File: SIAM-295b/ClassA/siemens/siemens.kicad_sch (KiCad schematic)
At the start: 113 parts, among them J1 PWR_IN, J2 Conn_01x08_Pin, J3 AUDIO_IN, J4 AUDIO_OUT, Q1 BC849, Q10 BCX56, Q11 BCX56, Q12 BC849, Q2 BCX56, Q3 BCX56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

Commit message: update ocb
added mounting holes, reduced width
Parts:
- removed R22: 1k2, Resistor_SMD:R_1206_3216Metric_Pad1.30x1.75mm_HandSolder, symbol Device:R
- added H1, H2, H4: MountingHole, MountingHole:MountingHole_3.2mm_M3_DIN965, symbol Mechanical:MountingHole
- added H3: MountingHole, MountingHole:MountingHole_3.2mm_M3_DIN965_Pad, symbol Mechanical:MountingHole_Pad
- added R43: 0R, Resistor_SMD:R_1206_3216Metric, symbol Device:R
- R18: value 1k3 -> 2k4
- R19: value 1k2 -> 100R
- R30: value 1k2 -> 2k4
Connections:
- net GND: now also R43.2
- net at R30.2: now also RV29.3
- new net: H3.1, R43.1

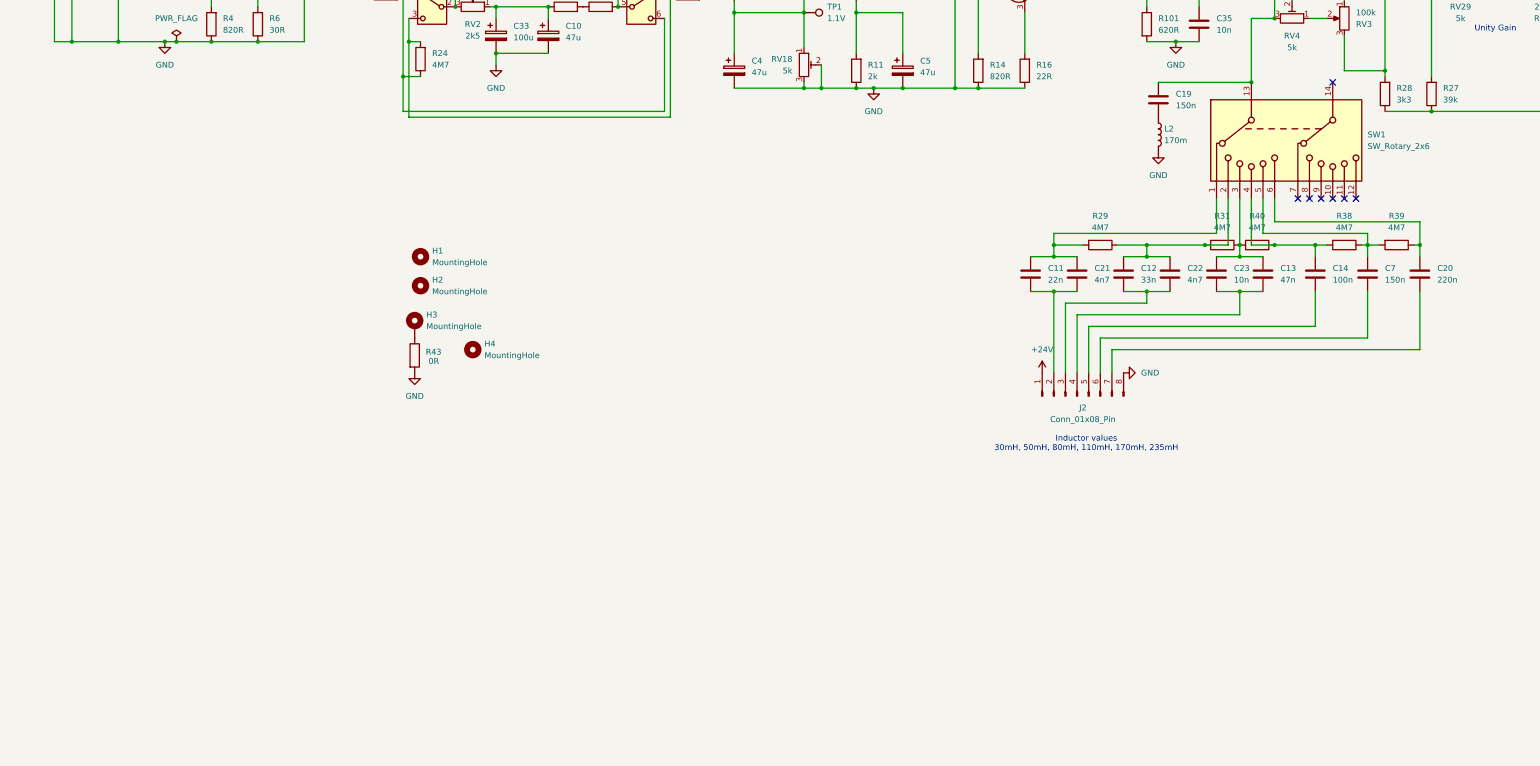
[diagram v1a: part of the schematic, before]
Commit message: added gyrator circuits
includes simulation
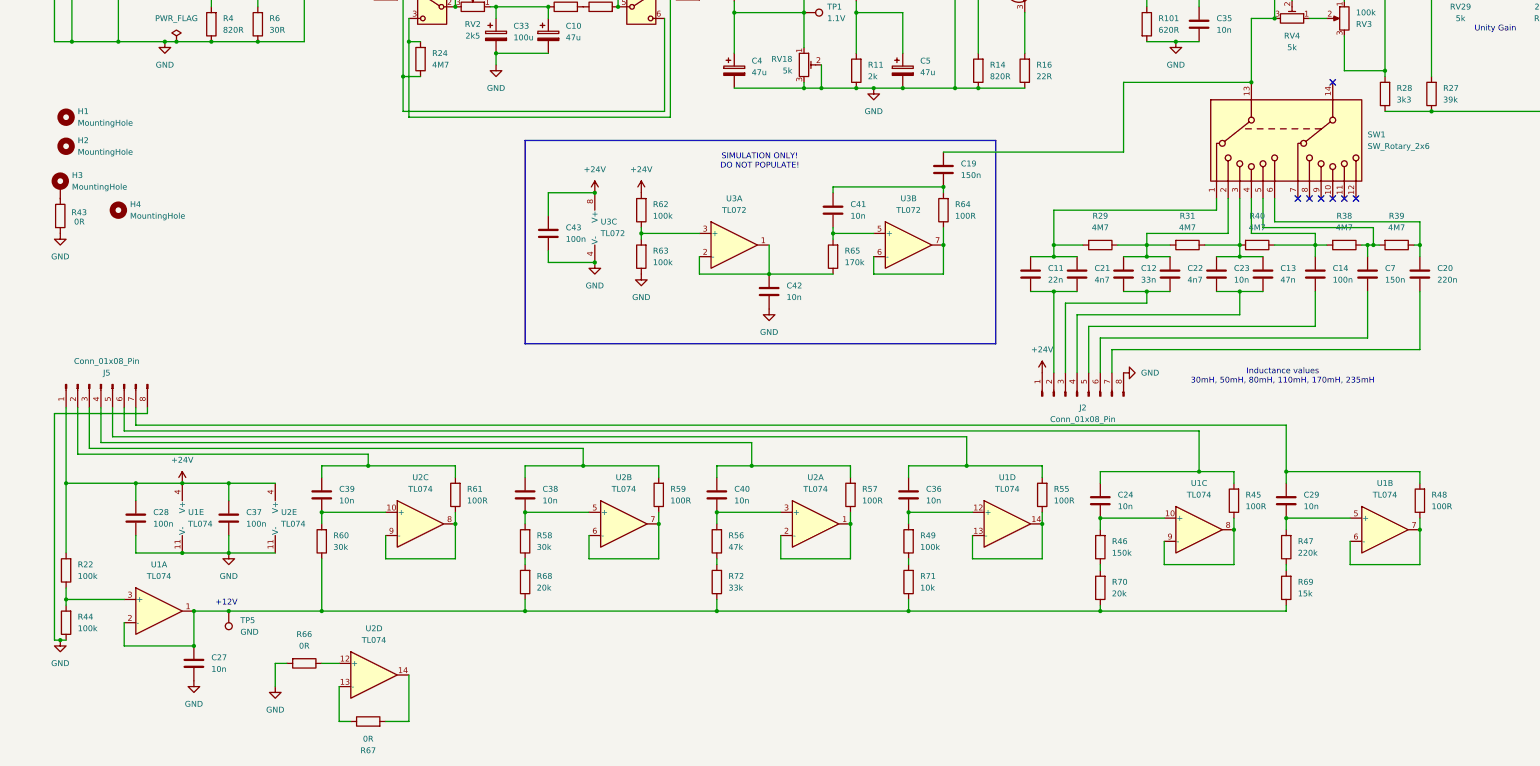
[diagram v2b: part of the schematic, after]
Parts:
- removed L2: 170m, symbol Device:L
- added C24, C27, C29, C36, C38, C39, C40, C41, C42: 10n, Capacitor_THT:C_Rect_L10.0mm_W4.0mm_P7.50mm_MKS4, symbol Device:C
- added C28, C37, C43: 100n, Capacitor_THT:C_Rect_L10.0mm_W4.0mm_P7.50mm_MKS4, symbol Device:C
- added J5: Conn_01x08_Pin, Connector_PinHeader_2.54mm:PinHeader_1x08_P2.54mm_Vertical, symbol Connector:Conn_01x08_Pin
- added R22, R44, R49, R62, R63: 100k, Resistor_SMD:R_1206_3216Metric_Pad1.30x1.75mm_HandSolder, symbol Device:R
- added R45, R48, R55, R57, R59, R61, R64: 100R, Resistor_SMD:R_1206_3216Metric_Pad1.30x1.75mm_HandSolder, symbol Device:R
- added R46: 150k, Resistor_SMD:R_1206_3216Metric_Pad1.30x1.75mm_HandSolder, symbol Device:R
- added R47: 220k, Resistor_SMD:R_1206_3216Metric_Pad1.30x1.75mm_HandSolder, symbol Device:R
- added R56: 47k, Resistor_SMD:R_1206_3216Metric_Pad1.30x1.75mm_HandSolder, symbol Device:R
- added R58, R60: 30k, Resistor_SMD:R_1206_3216Metric_Pad1.30x1.75mm_HandSolder, symbol Device:R
- added R65: 170k, Resistor_SMD:R_1206_3216Metric_Pad1.30x1.75mm_HandSolder, symbol Device:R
- added R66, R67: 0R, Resistor_SMD:R_1206_3216Metric_Pad1.30x1.75mm_HandSolder, symbol Device:R
- added R68, R70: 20k, Resistor_SMD:R_1206_3216Metric_Pad1.30x1.75mm_HandSolder, symbol Device:R
- added R69: 15k, Resistor_SMD:R_1206_3216Metric_Pad1.30x1.75mm_HandSolder, symbol Device:R
- added R71: 10k, Resistor_SMD:R_1206_3216Metric_Pad1.30x1.75mm_HandSolder, symbol Device:R
- added R72: 33k, Resistor_SMD:R_1206_3216Metric_Pad1.30x1.75mm_HandSolder, symbol Device:R
- added TP5: GND, TestPoint:TestPoint_THTPad_1.0x1.0mm_Drill0.5mm, symbol Connector:TestPoint
- added U1, U2: TL074, Package_SO:SOIC-14_3.9x8.7mm_P1.27mm, symbol Amplifier_Operational:TL074
- added U3: TL072, symbol Amplifier_Operational:TL072
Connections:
- net +24V: now also C28.1, C37.1, C43.1, J5.1 (Pin_1), R22.2, R62.2, U1.4 (V+), U2.4 (V+), U3.8 (V+)
- net GND: now also C27.2, C28.2, C37.2, C42.2, C43.2, J5.8 (Pin_8), R44.1, R63.1, R66.2, U1.11 (V-), U2.11 (V-), U3.4 (V-)
- net at C19.2: now also C41.1, R64.2
- new net: R59.1, U2.6 (-), U2.7
- new net: C38.1, J5.3 (Pin_3), R59.2
- new net: C41.2, R65.2, U3.5 (+)
- new net: R64.1, U3.6 (-), U3.7
- new net: C24.2, R46.2, U1.10 (+)
- new net: R45.1, U1.8, U1.9 (-)
- new net: C27.1, R60.1, R68.1, R69.1, R70.1, R71.1, R72.1, TP5.1, U1.1, U1.2 (-)
- new net: C39.2, R60.2, U2.10 (+)
- new net: C29.1, J5.7 (Pin_7), R48.2
- new net: C29.2, R47.2, U1.5 (+)
- new net: R48.1, U1.6 (-), U1.7
- new net: C40.1, J5.4 (Pin_4), R57.2
- new net: C40.2, R56.2, U2.3 (+)
- new net: C38.2, R58.2, U2.5 (+)
- new net: C24.1, J5.6 (Pin_6), R45.2
- new net: R47.1, R69.2
- new net: C42.1, R65.1, U3.1, U3.2 (-)
- new net: R62.1, R63.2, U3.3 (+)
- new net: R67.1, U2.13 (-)
- new net: R67.2, U2.14
- new net: R49.1, R71.2
- new net: C36.2, R49.2, U1.12 (+)
- new net: R57.1, U2.1, U2.2 (-)
- new net: C39.1, J5.2 (Pin_2), R61.2
- new net: C36.1, J5.5 (Pin_5), R55.2
- new net: R66.1, U2.12 (+)
- new net: R61.1, U2.8, U2.9 (-)
- new net: R55.1, U1.13 (-), U1.14
- new net: R56.1, R72.2
- new net: R46.1, R70.2
- new net: R58.1, R68.2
- new net: R22.1, R44.2, U1.3 (+)
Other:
- note added: "+12V"
- note added: "Inductance values 30mH, 50mH, 80mH, 110mH, 170mH, 235mH"
- note added: "SIMULATION ONLY! DO NOT POPULATE!"
- note removed: "Inductor values 30mH, 50mH, 80mH, 110mH, 170mH, 235mH"
- moved on the sheet: C19, H1, H2, H3, H4, R31, R43

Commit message: updated footprints
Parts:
- C27, C28, C37, C43: footprint Capacitor_THT:C_Rect_L10.0mm_W4.0mm_P7.50mm_MKS4 -> Capacitor_SMD:C_0805_2012Metric_Pad1.18x1.45mm_HandSolder
- C9: footprint Capacitor_SMD:C_0805_2012Metric -> Capacitor_SMD:C_0805_2012Metric_Pad1.18x1.45mm_HandSolder
- R43: footprint Resistor_SMD:R_1206_3216Metric -> Resistor_SMD:R_1206_3216Metric_Pad1.30x1.75mm_HandSolder
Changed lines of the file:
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@@
 			)
 		)
-		(property "Footprint" "Resistor_SMD:R_1206_3216Metric"
+		(property "Footprint" "Resistor_SMD:R_1206_3216Metric_Pad1.30x1.75mm_HandSolder"
 			(at 19.812 158.75 90)
 			(effects
@@
 			)
 		)
-		(property "Footprint" "Capacitor_THT:C_Rect_L10.0mm_W4.0mm_P7.50mm_MKS4"
+		(property "Footprint" "Capacitor_SMD:C_0805_2012Metric_Pad1.18x1.45mm_HandSolder"
 			(at 129.2352 166.37 0)
 			(effects
@@
 			)
 		)
-		(property "Footprint" "Capacitor_SMD:C_0805_2012Metric"
+		(property "Footprint" "Capacitor_SMD:C_0805_2012Metric_Pad1.18x1.45mm_HandSolder"
 			(at 185.1152 90.17 0)
 			(effects
@@
 			)
 		)
-		(property "Footprint" "Capacitor_THT:C_Rect_L10.0mm_W4.0mm_P7.50mm_MKS4"
+		(property "Footprint" "Capacitor_SMD:C_0805_2012Metric_Pad1.18x1.45mm_HandSolder"
 			(at 39.0652 228.6 0)
 			(effects
@@
 			)
 		)
-		(property "Footprint" "Capacitor_THT:C_Rect_L10.0mm_W4.0mm_P7.50mm_MKS4"
+		(property "Footprint" "Capacitor_SMD:C_0805_2012Metric_Pad1.18x1.45mm_HandSolder"
 			(at 51.7652 260.35 0)
 			(effects
@@
 			)
 		)
-		(property "Footprint" "Capacitor_THT:C_Rect_L10.0mm_W4.0mm_P7.50mm_MKS4"
+		(property "Footprint" "Capacitor_SMD:C_0805_2012Metric_Pad1.18x1.45mm_HandSolder"
 			(at 59.3852 228.6 0)
 			(effects
